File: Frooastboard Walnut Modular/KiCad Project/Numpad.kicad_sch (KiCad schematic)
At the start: 63 parts, among them J19 Conn_01x15_Male, J20 Conn_01x06_Male, J21 Conn_01x13_Male, M1 Frooastboard_MM2040

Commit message: fix some issues
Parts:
- J19: value Conn_01x15_Male -> Conn_01x15_Pin; symbol Connector:Conn_01x15_Male -> Connector:Conn_01x15_Pin
- J20: symbol Connector:Conn_01x06_Male -> Connector:Conn_01x06_Pin
- J21: symbol Connector:Conn_01x13_Male -> Connector:Conn_01x13_Pin
- MX17: symbol MX_Alps_Hybrid:MX-NoLED -> MX_Alps_Hybrid:MX-LED
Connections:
- net CS13: no longer D58.1 (K), D76.5 (B-), D77.5 (B-), D78.5 (B-), D79.5 (B-), J20.3 (Pin_3), M1.41 (SW6)
- net CS2: now also MX17.3 (LED)
- net SW6: now reaches D80.5 (B-), D81.5 (B-), D82.5 (B-), D83.5 (B-)
- net SW6: now also D58.1 (K), D76.5 (B-), D77.5 (B-), D78.5 (B-), D79.5 (B-), J20.3 (Pin_3), M1.41 (SW6), MX17.4 (LEDGND)
- no-connect marks 20 -> 22

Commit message: updates or something like that
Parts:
- added D100, D101, D103, D104, D106, D111, D99: RGB_LED_6_Pin, Frooastboard Footprints:Everlight 99-235, symbol Frooastboard Symbols:RGB_LED_6_Pin
- added D91, D92: D_Small, Diode_SMD:D_0805_2012Metric, symbol Device:D_Small
- added MX145: Small Minus, MX_Only:MXOnly-1U-NoLED, symbol MX_Alps_Hybrid:MX-NoLED
- added MX148: Num 00, MX_Only:MXOnly-1U-NoLED, symbol MX_Alps_Hybrid:MX-NoLED
- added MX149: Num 0, MX_Only:MXOnly-1U-NoLED, symbol MX_Alps_Hybrid:MX-NoLED
- added MX150: Plus, MX_Only:MXOnly-1U-NoLED, symbol MX_Alps_Hybrid:MX-NoLED
- MX35, MX37: footprint MX_Only:MXOnly-2U-VerticalStabilizers-NoLED -> MX_Only:MXOnly-2U-ReversedVerticalStabilizers-NoLED
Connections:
- net COL8: now also MX148.1 (COL), MX149.1 (COL)
- net COL9: now also MX145.1 (COL), MX150.1 (COL)
- net CS10: now also D99.2 (G+), D99.4 (R+), D99.6 (B+)
- net CS11: now also D100.2 (G+), D100.4 (R+), D100.6 (B+)
- net CS6: now also D111.2 (G+), D111.4 (R+), D111.6 (B+)
- net CS7: now also D103.2 (G+), D103.4 (R+), D103.6 (B+)
- net CS8: now also D104.2 (G+), D104.4 (R+), D104.6 (B+)
- net CS9: now also D106.2 (G+), D106.4 (R+), D106.6 (B+)
- net ROW5: now also D91.1 (K)
- net ROW9: now also D92.1 (K)
- net SW4: now also D100.1 (G-), D101.1 (G-), D103.1 (G-), D104.1 (G-), D106.1 (G-), D111.1 (G-), D99.1 (G-)
- net SW5: now also D100.3 (R-), D101.3 (R-), D103.3 (R-), D104.3 (R-), D106.3 (R-), D111.3 (R-), D99.3 (R-)
- net SW6: now also D100.5 (B-), D101.5 (B-), D103.5 (B-), D104.5 (B-), D106.5 (B-), D111.5 (B-), D99.5 (B-)
- net at D51.2 (A), MX21.2 (ROW): now also MX149.2 (ROW)
- net CS12: now reaches M1.59 (CS12)
- net CS12: now also D101.2 (G+), D101.4 (R+), D101.6 (B+)
- net at D67.2 (A), MX35.2 (ROW): now also MX150.2 (ROW)
- new net: D92.2 (A), MX148.2 (ROW)
- new net: D91.2 (A), MX145.2 (ROW)
- no-connect marks 22 -> 20

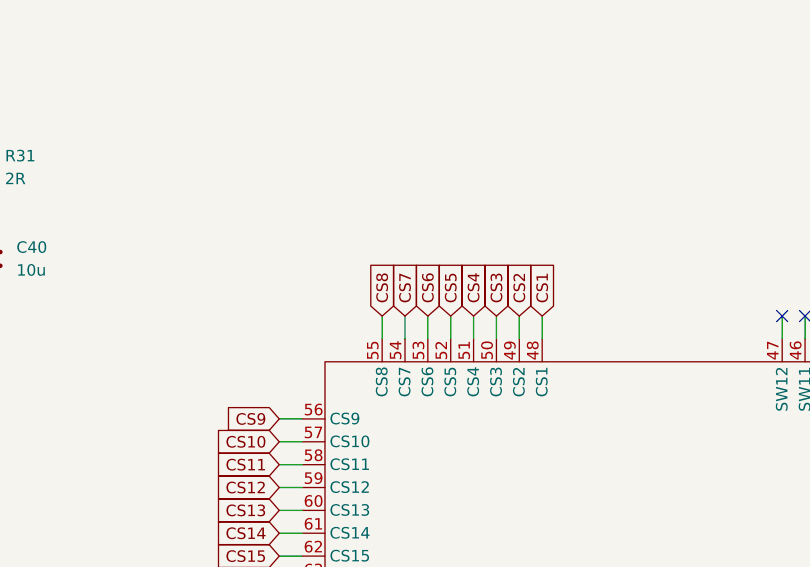
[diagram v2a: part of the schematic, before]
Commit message: fix symbols and remove lck
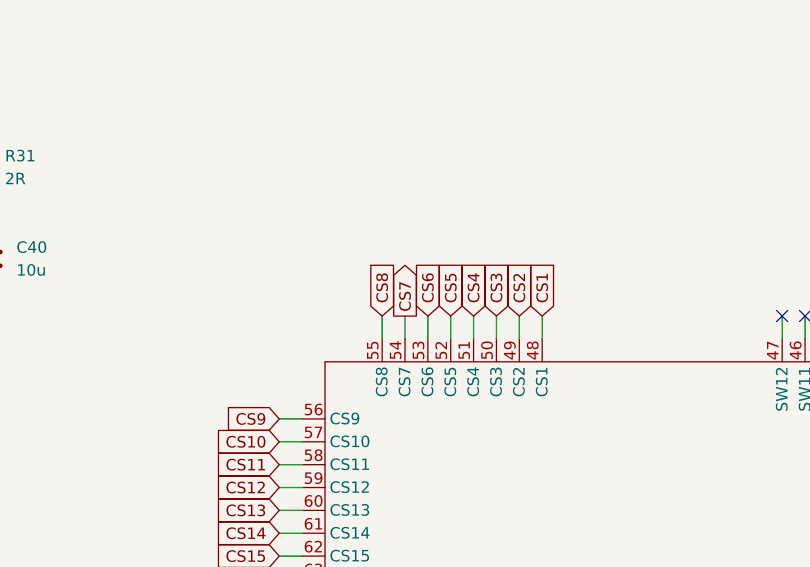
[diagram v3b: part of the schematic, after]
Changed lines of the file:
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@@
     )
   )
-  (global_label "CS7" (shape input) (at 318.77 138.43 90) (fields_autoplaced)
+  (global_label "CS7" (shape output) (at 318.77 138.43 90) (fields_autoplaced)
     (effects (font (size 1.27 1.27)) (justify left))
     (property "Intersheetrefs" "${INTERSHEET_REFS}" (at 318.77 131.7558 90)

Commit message: almost finished bus stuff connector fpc
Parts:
- removed J19: Conn_01x15_Pin, Connector_PinHeader_1.27mm:PinHeader_1x15_P1.27mm_Vertical, symbol Connector:Conn_01x15_Pin
- removed J20: Conn_01x06_Male, Connector_PinHeader_1.27mm:PinHeader_1x06_P1.27mm_Vertical, symbol Connector:Conn_01x06_Pin
- removed J21: Conn_01x13_Male, Connector_PinHeader_1.27mm:PinHeader_1x13_P1.27mm_Vertical, symbol Connector:Conn_01x13_Pin
- removed M1: Frooastboard_MM2040, Frooastboard Footprints:MM2040, symbol Frooastboard Symbols:Frooastboard_MM2040
- added M2: Frooastboard_MM2040, Frooastboard Footprints:MM2040, symbol Frooastboard Symbols:Frooastboard_MM2040
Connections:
- net +5V: now also M2.3 (5V), M2.7 (5V)
- net CS2: no longer D44.2 (G+), D44.4 (R+), D44.6 (B+), D58.2 (A)
- net GND: now also M2.1 (GND), M2.34 (GND), M2.6 (GND)
- net SW6: no longer D100.5 (B-), D101.5 (B-), D103.5 (B-), D104.5 (B-), D106.5 (B-), D111.5 (B-), D58.1 (K), D76.5 (B-), D77.5 (B-), D78.5 (B-), D79.5 (B-), D80.5 (B-), D81.5 (B-), D82.5 (B-), D83.5 (B-), D99.5 (B-)
- net COL8 renamed np_col8
- net np_col8: now also M2.20 (COL8)
- net COL9 renamed np_col9
- net np_col9: now also M2.21 (COL9)
- net CS1 renamed np_cs1
- net np_cs1: now also D111.2 (G+), D111.4 (R+), D111.6 (B+), M2.48 (CS1)
- net CS10 renamed np_cs10
- net np_cs10: now also M2.57 (CS10); no longer D99.2 (G+), D99.4 (R+), D99.6 (B+)
- net CS11 renamed np_cs11
- net np_cs11: now also M2.58 (CS11); no longer D100.2 (G+), D100.4 (R+), D100.6 (B+)
- net CS12 renamed np_cs7
- net np_cs7: now also D71.2 (G+), D71.4 (R+), D71.6 (B+), M2.54 (CS7)
- net CS13 renamed np_cs13
- net np_cs13: now also M2.60 (CS13)
- net CS14 renamed np_cs14
- net np_cs14: now also M2.61 (CS14)
- net CS15 renamed np_cs15
- net np_cs15: now also M2.62 (CS15)
- net CS16 renamed np_cs16
- net np_cs16: now also M2.63 (CS16)
- net CS3 renamed np_cs3
- net np_cs3: now also D104.2 (G+), D104.4 (R+), D104.6 (B+), M2.50 (CS3)
- net CS4 renamed np_cs4
- net np_cs4: now also D106.2 (G+), D106.4 (R+), D106.6 (B+), M2.51 (CS4)
- net CS5 renamed np_cs5
- net np_cs5: now also D99.2 (G+), D99.4 (R+), D99.6 (B+), M2.52 (CS5)
- net CS6 renamed np_cs6
- net np_cs6: now also D100.2 (G+), D100.4 (R+), D100.6 (B+), M2.53 (CS6); no longer D111.2 (G+), D111.4 (R+), D111.6 (B+)
- net CS7 renamed np_cs2
- net np_cs2: now also D44.2 (G+), D44.4 (R+), D44.6 (B+), D58.2 (A), M2.49 (CS2); no longer D71.2 (G+), D71.4 (R+), D71.6 (B+)
- net CS8 renamed np_cs8
- net np_cs8: now also M2.55 (CS8); no longer D104.2 (G+), D104.4 (R+), D104.6 (B+)
- net CS9 renamed np_cs9
- net np_cs9: now also M2.56 (CS9); no longer D106.2 (G+), D106.4 (R+), D106.6 (B+)
- net D+ renamed np_dp
- net np_dp: now also M2.8 (D+)
- net D- renamed np_dn
- net np_dn: now also M2.9 (D-)
- net ROW0 renamed np_row0
- net np_row0: now also M2.22 (ROW0)
- net ROW1 renamed np_row1
- net np_row1: now also M2.23 (ROW1)
- net ROW2 renamed np_row2
- net np_row2: now also M2.24 (ROW2)
- net ROW3 renamed np_row3
- net np_row3: now also M2.25 (ROW3)
- net ROW4 renamed np_row4
- net np_row4: now also M2.26 (ROW4)
- net ROW5 renamed np_row5
- net np_row5: now also M2.27 (ROW5)
- net ROW6 renamed np_row6
- net np_row6: now also M2.28 (ROW6)
- net ROW7 renamed np_row7
- net np_row7: now also M2.29 (ROW7)
- net ROW8 renamed np_row8
- net np_row8: now also M2.30 (ROW8)
- net ROW9 renamed np_row9
- net np_row9: now also M2.31 (ROW9)
- net SW4 renamed np_sw4
- net np_sw4: now also M2.39 (SW4); no longer D100.1 (G-), D101.1 (G-), D103.1 (G-), D104.1 (G-), D106.1 (G-), D111.1 (G-), D99.1 (G-)
- net SW5 renamed np_sw5
- net np_sw5: now also M2.40 (SW5); no longer D100.3 (R-), D101.3 (R-), D103.3 (R-), D104.3 (R-), D106.3 (R-), D111.3 (R-), D99.3 (R-)
- net SW7 renamed np_sw7
- net np_sw7: now also M2.42 (SW7)
- net SW8 renamed np_sw8
- net np_sw8: now also M2.43 (SW8)
- net SW9 renamed np_sw9
- net np_sw9: now also M2.44 (SW9)
- new net +3.3V: M2.2 (3V3), M2.35 (3V3)
- new net np_gpio1: M2.4 (GPIO1)
- new net np_gpio2: M2.5 (GPIO2)
- new net np_sw1: D100.1 (G-), D101.1 (G-), D103.1 (G-), D104.1 (G-), D106.1 (G-), D111.1 (G-), D99.1 (G-)
- new net np_sw2: D100.3 (R-), D101.3 (R-), D103.3 (R-), D104.3 (R-), D106.3 (R-), D111.3 (R-), D99.3 (R-)
- new net np_sw3: D100.5 (B-), D101.5 (B-), D103.5 (B-), D104.5 (B-), D106.5 (B-), D111.5 (B-), D99.5 (B-)
- new net np_sw6: D58.1 (K), D76.5 (B-), D77.5 (B-), D78.5 (B-), D79.5 (B-), D80.5 (B-), D81.5 (B-), D82.5 (B-), D83.5 (B-), M2.41 (SW6)
- no-connect marks 20 -> 19
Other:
- moved on the sheet: D100, D101, D103, D104, D106, D111, D43, D44, D45, D46, D53, D58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
